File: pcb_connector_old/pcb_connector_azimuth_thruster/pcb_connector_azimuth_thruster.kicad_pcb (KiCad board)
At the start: 2 copper layers, 43.3 x 43.3 mm, 15 parts

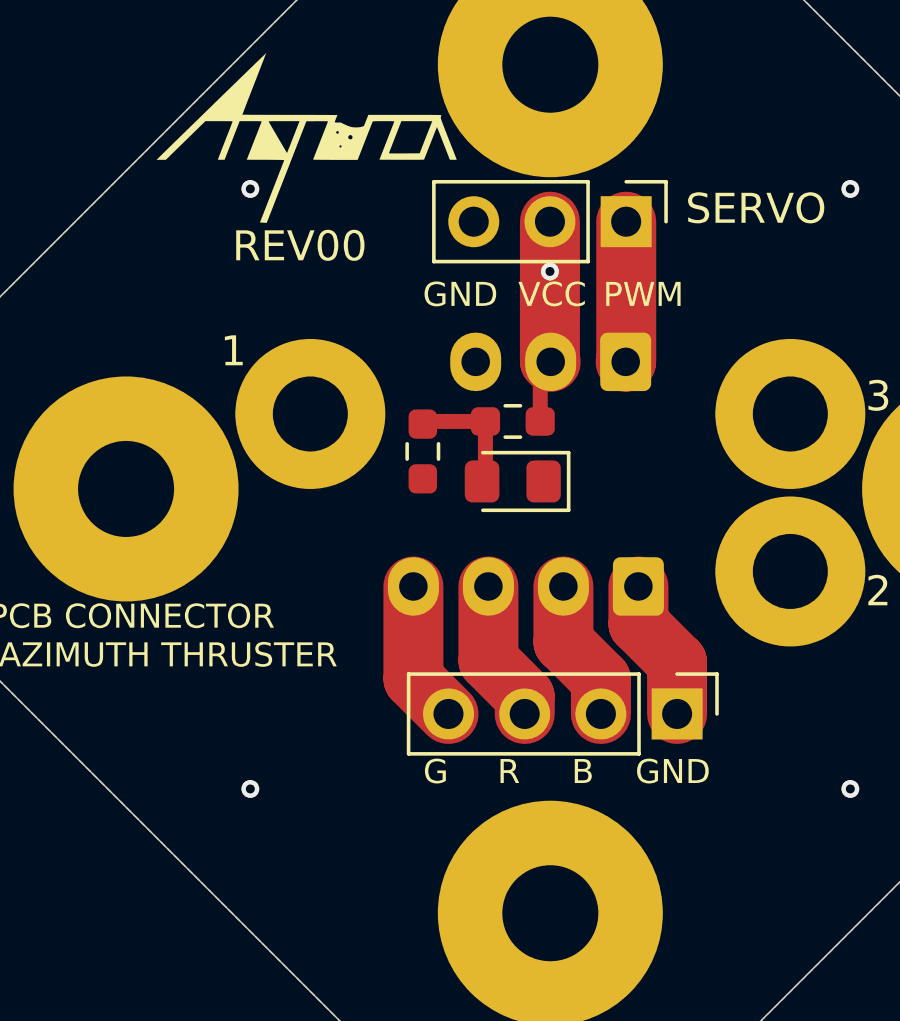
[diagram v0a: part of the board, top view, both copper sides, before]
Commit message: 旧基板防水をpcb_connector_oldに移動
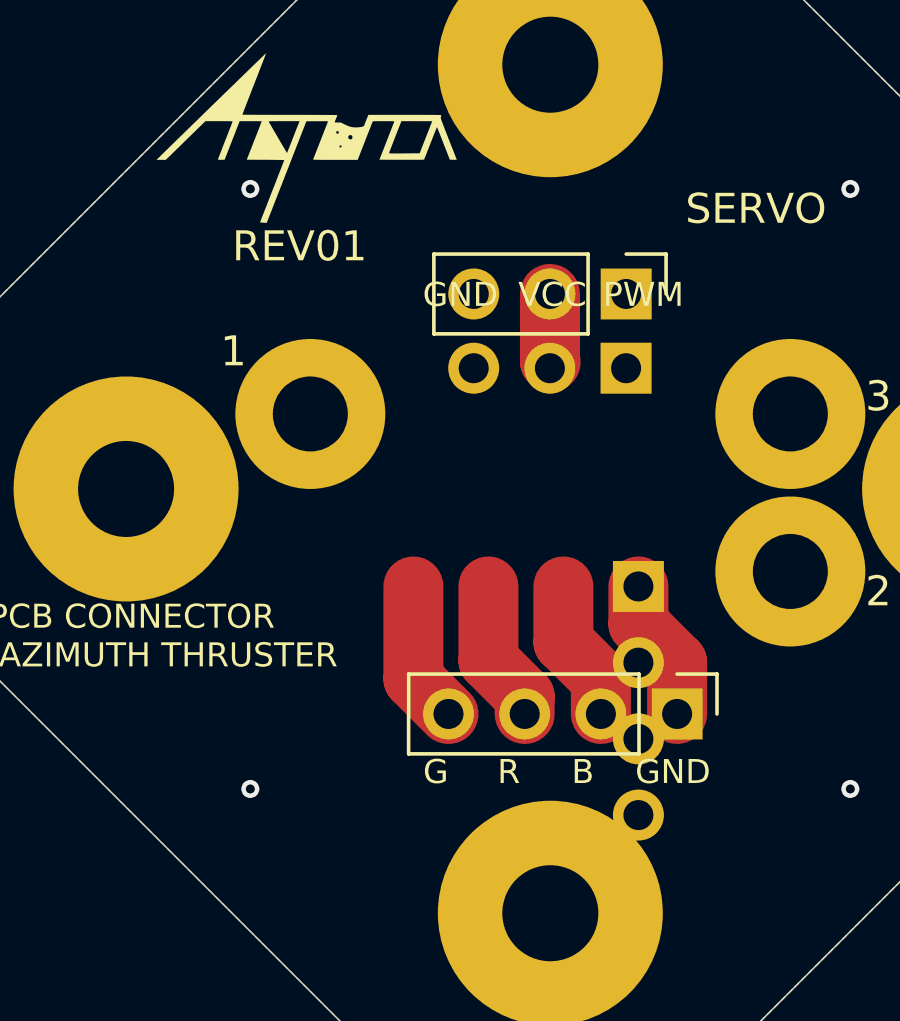
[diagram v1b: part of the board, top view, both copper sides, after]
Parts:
- removed R2: 1k, Resistor_SMD:R_0603_1608Metric_Pad0.98x0.95mm_HandSolder
- removed R4: 2.2k, Resistor_SMD:R_0603_1608Metric_Pad0.98x0.95mm_HandSolder
- removed SERVO_OK_OUTER1: GREEN, LED_SMD:LED_0805_2012Metric_Pad1.15x1.40mm_HandSolder
- RGBLED1: footprint Connector_JST:JST_XA_B04B-XASK-1_1x04_P2.50mm_Vertical -> Connector_PinHeader_2.54mm:PinHeader_1x04_P2.54mm_Vertical
- SERVO1: footprint Connector_JST:JST_XA_B03B-XASK-1_1x03_P2.50mm_Vertical -> Connector_PinSocket_2.54mm:PinSocket_1x03_P2.54mm_Vertical
- moved SERVO2 2.41 mm to (92.2, 61.0)
- moved SERVO1 0.21 mm to (92.2, 63.5), turned to 90 degrees
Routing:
- net Net-(SERVO1-Pin_1): track 4.68 -> 0.00 mm
- net Net-(SERVO_OK_OUTER1-A): track 4.13 -> 0.00 mm
- net +7V: track 7.98 -> 3.93 mm, vias 1 -> 0
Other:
- board text added: "REV01"
- board text removed: "REV00"
